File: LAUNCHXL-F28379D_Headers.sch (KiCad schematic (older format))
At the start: 10 parts, among them J1 Conn_01x10_Female, U1 AMP_DUE_SCH, U3 SN74AS08N, U4 LoRa

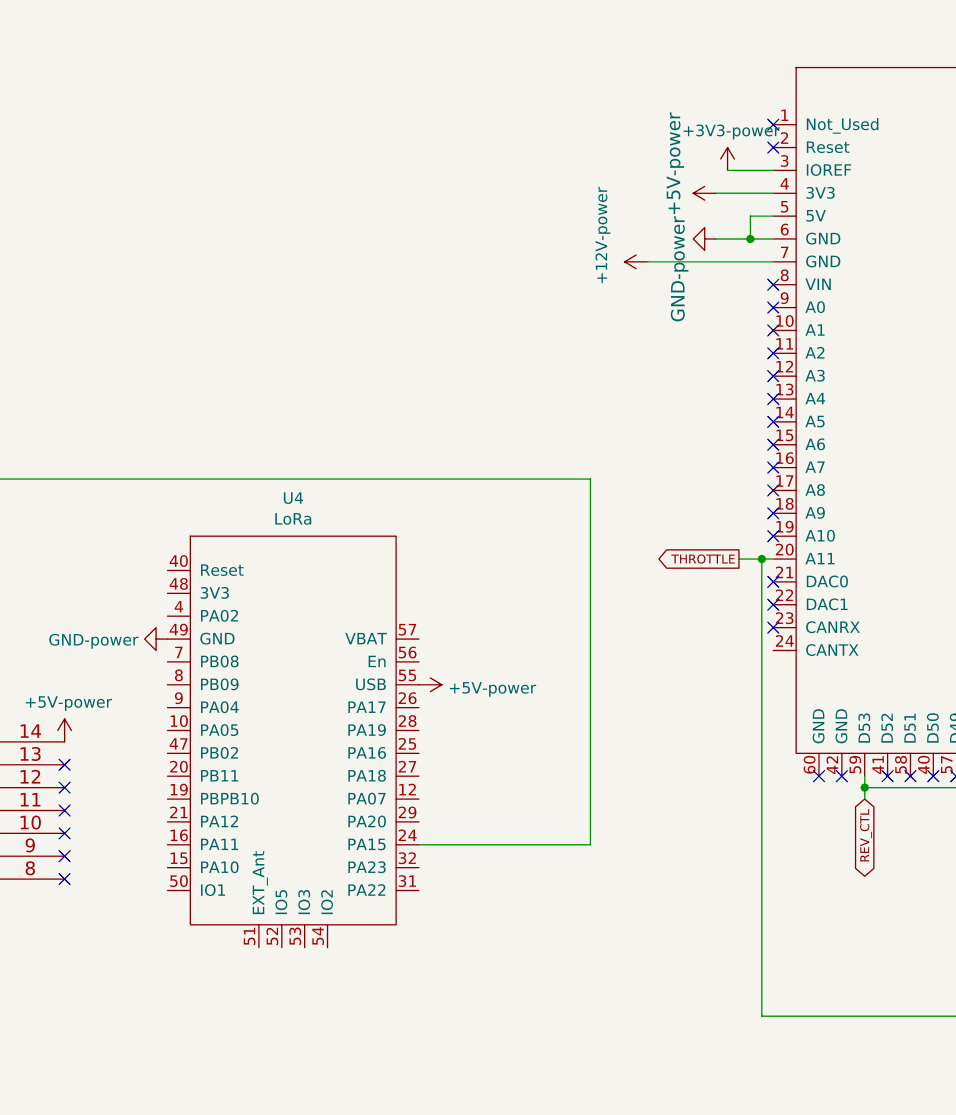
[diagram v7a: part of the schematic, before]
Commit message: updated trace width
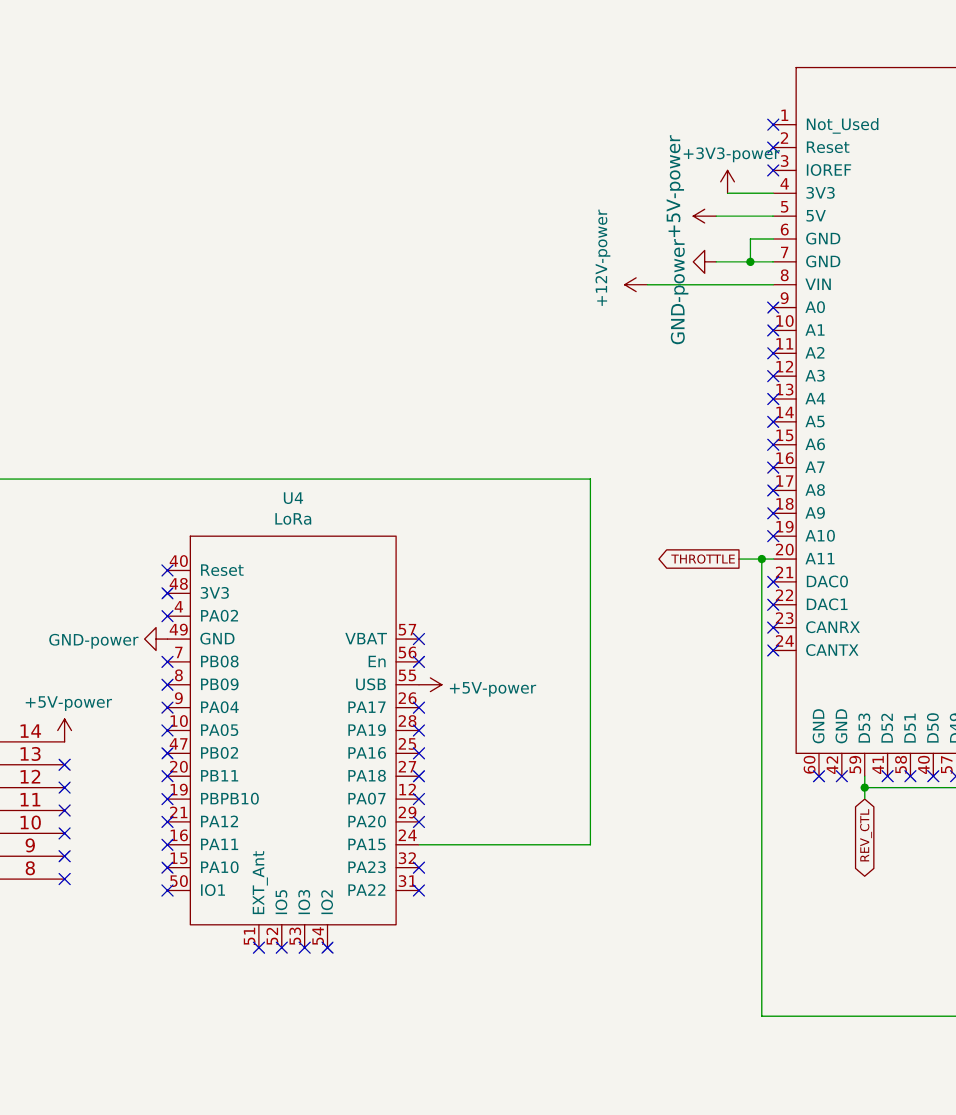
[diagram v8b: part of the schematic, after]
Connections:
- net +12V: now also U1.8 (VIN); no longer U1.7 (GND)
- net +3V3: now also U1.4 (3V3); no longer U1.3 (IOREF)
- net +5V: now also U1.5 (5V); no longer U1.4 (3V3)
- net GND: now also U1.7 (GND); no longer U1.5 (5V)
- no-connect marks 77 -> 106
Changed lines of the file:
@@
 L PCB_2020-rescue:+12V-power #PWR01
 U 1 1 5E686230
-P 6050 2200
-F 0 "#PWR01" H 6050 2050 50  0001 C CNN
-F 1 "+12V-power" H 5950 2400 50  0000 L CNN
-F 2 "" H 6050 2200 50  0001 C CNN
-F 3 "" H 6050 2200 50  0001 C CNN
-	1    6050 2200
+P 6050 2300
+F 0 "#PWR01" H 6050 2150 50  0001 C CNN
+F 1 "+12V-power" H 5950 2500 50  0000 L CNN
+F 2 "" H 6050 2300 50  0001 C CNN
+F 3 "" H 6050 2300 50  0001 C CNN
+	1    6050 2300
 	0    -1   -1   0
 $EndComp
@@
 L PCB_2020-rescue:+5V-power #P+?
 U 1 1 5E684B6F
-P 6350 1900
+P 6350 2000
 AR Path="/5E684B6F" Ref="#P+?"  Part="1"
 AR Path="/5DF27589/5E684B6F" Ref="#P+06"  Part="1"
-F 0 "#P+06" H 6350 1900 50  0001 C CNN
-F 1 "+5V-power" H 6250 2050 59  0000 L BNN
-F 2 "" H 6350 1900 50  0001 C CNN
-F 3 "" H 6350 1900 50  0001 C CNN
-	1    6350 1900
+F 0 "#P+06" H 6350 2000 50  0001 C CNN
+F 1 "+5V-power" H 6250 2150 59  0000 L BNN
+F 2 "" H 6350 2000 50  0001 C CNN
+F 3 "" H 6350 2000 50  0001 C CNN
+	1    6350 2000
 	0    -1   -1   0
 $EndComp
@@
 L PCB_2020-rescue:GND-power #GND?
 U 1 1 5E681F81
-P 6350 2100
+P 6350 2200
 AR Path="/5E681F81" Ref="#GND?"  Part="1"
 AR Path="/5DF27589/5E681F81" Ref="#GND04"  Part="1"
-F 0 "#GND04" H 6350 2100 50  0001 C CNN
-F 1 "GND-power" H 6250 1900 59  0000 L BNN
-F 2 "" H 6350 2100 50  0001 C CNN
-F 3 "" H 6350 2100 50  0001 C CNN
-	1    6350 2100
+F 0 "#GND04" H 6350 2200 50  0001 C CNN
+F 1 "GND-power" H 6250 2000 59  0000 L BNN
+F 2 "" H 6350 2200 50  0001 C CNN
+F 3 "" H 6350 2200 50  0001 C CNN
+	1    6350 2200
 	0    1    1    0
 $EndComp
@@
 Wire Wire Line
 	3700 7050 4400 7050
-$Comp
-L PCB_2020:AMP_DUE_SCH U1
-U 1 1 5F87F561
-P 8550 3050
-F 0 "U1" H 8550 4915 50  0000 C CNN
-F 1 "AMP_DUE_SCH" H 8550 4824 50  0000 C CNN
-F 2 "Drivetrain_control:Arduino DUE" H 8550 3050 50  0001 C CNN
-F 3 "" H 9100 2950 50  0001 C CNN
-	1    8550 3050
-	1    0    0    -1
-$EndComp
 Wire Wire Line
 	6450 3500 6550 3500
 Wire Wire Line
-	6350 1900 6600 1900
-Wire Wire Line
-	6350 2100 6500 2100
-Wire Wire Line
-	6500 2100 6500 2000
-Wire Wire Line
-	6500 2000 6600 2000
-Connection ~ 6500 2100
+	6350 2000 6600 2000
+Wire Wire Line
+	6350 2200 6500 2200
+Wire Wire Line
+	6500 2200 6500 2100
 Wire Wire Line
 	6500 2100 6600 2100
-Wire Wire Line
-	6050 2200 6600 2200
+Connection ~ 6500 2200
+Wire Wire Line
+	6500 2200 6600 2200
+Wire Wire Line
+	6050 2300 6600 2300
 NoConn ~ 6600 1600
 NoConn ~ 6600 1700
-NoConn ~ 6600 2300
 NoConn ~ 6600 2400
 NoConn ~ 6600 2500
@@
 L PCB_2020-rescue:+3V3-power #PWR0108
 U 1 1 5FAB7823
-P 6400 1800
-F 0 "#PWR0108" H 6400 1650 50  0001 C CNN
-F 1 "+3V3-power" H 6415 1973 50  0000 C CNN
-F 2 "" H 6400 1800 50  0001 C CNN
-F 3 "" H 6400 1800 50  0001 C CNN
-	1    6400 1800
-	1    0    0    -1
-$EndComp
-Wire Wire Line
-	6400 1800 6600 1800
+P 6400 1900
+F 0 "#PWR0108" H 6400 1750 50  0001 C CNN
+F 1 "+3V3-power" H 6415 2073 50  0000 C CNN
+F 2 "" H 6400 1900 50  0001 C CNN
+F 3 "" H 6400 1900 50  0001 C CNN
+	1    6400 1900
+	1    0    0    -1
+$EndComp
+Wire Wire Line
+	6400 1900 6600 1900
 $Comp
 L PCB_2020-rescue:GND-power #PWR0109
@@
 	950  3800 950  4400
 Wire Wire Line
-	10500 3200 10600 3200
-Wire Wire Line
-	10500 3300 10600 3300
-Wire Wire Line
 	5800 4750 5050 4750
 Wire Wire Line
@@
 	0    1    1    0
 $EndComp
+NoConn ~ 6600 1800
+NoConn ~ 6600 3900
+NoConn ~ 5050 3850
+NoConn ~ 5050 3950
+NoConn ~ 5050 4150
+NoConn ~ 5050 4250
+NoConn ~ 5050 4350
+NoConn ~ 5050 4450
+NoConn ~ 5050 4550
+NoConn ~ 5050 4650
+NoConn ~ 5050 4850
+NoConn ~ 5050 4950
+NoConn ~ 4650 5200
+NoConn ~ 4550 5200
+NoConn ~ 4450 5200
+NoConn ~ 4350 5200
+NoConn ~ 3950 4950
+NoConn ~ 3950 4850
+NoConn ~ 3950 4750
+NoConn ~ 3950 4650
+NoConn ~ 3950 4550
+NoConn ~ 3950 4450
+NoConn ~ 3950 3550
+NoConn ~ 3950 3650
+NoConn ~ 3950 3750
+NoConn ~ 3950 3950
+NoConn ~ 3950 4050
+NoConn ~ 3950 4150
+NoConn ~ 3950 4250
+NoConn ~ 3950 4350
+$Comp
+L PCB_2020:AMP_DUE_SCH U1
+U 1 1 5F87F561
+P 8550 3050
+F 0 "U1" H 8550 4915 50  0000 C CNN
+F 1 "AMP_DUE_SCH" H 8550 4824 50  0000 C CNN
+F 2 "Drivetrain_control:Arduino DUE" H 8550 3050 50  0001 C CNN
+F 3 "" H 9100 2950 50  0001 C CNN
+	1    8550 3050
+	1    0    0    -1
+$EndComp
+Wire Wire Line
+	10500 3200 10600 3200
+Wire Wire Line
+	10500 3300 10600 3300
 $EndSCHEMATC
